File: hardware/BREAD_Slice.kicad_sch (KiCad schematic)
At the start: 14 parts, among them J1 Conn_01x10_Female

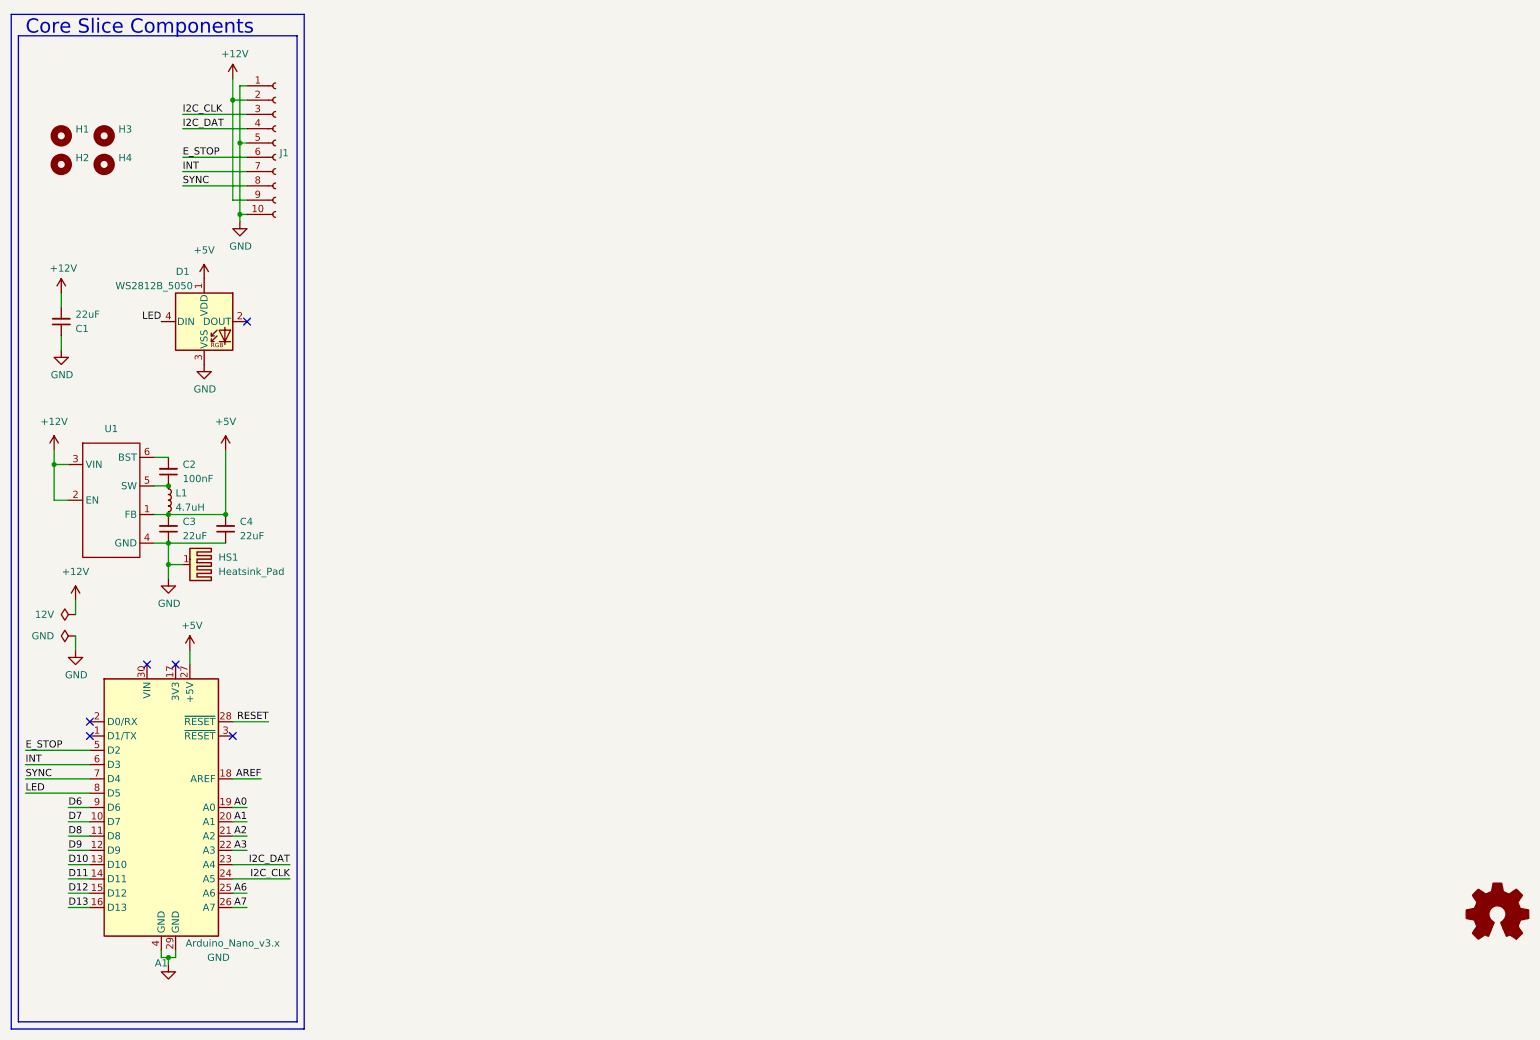
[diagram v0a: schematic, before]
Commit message: clear erc and drc but this board needs some rebuild help long term
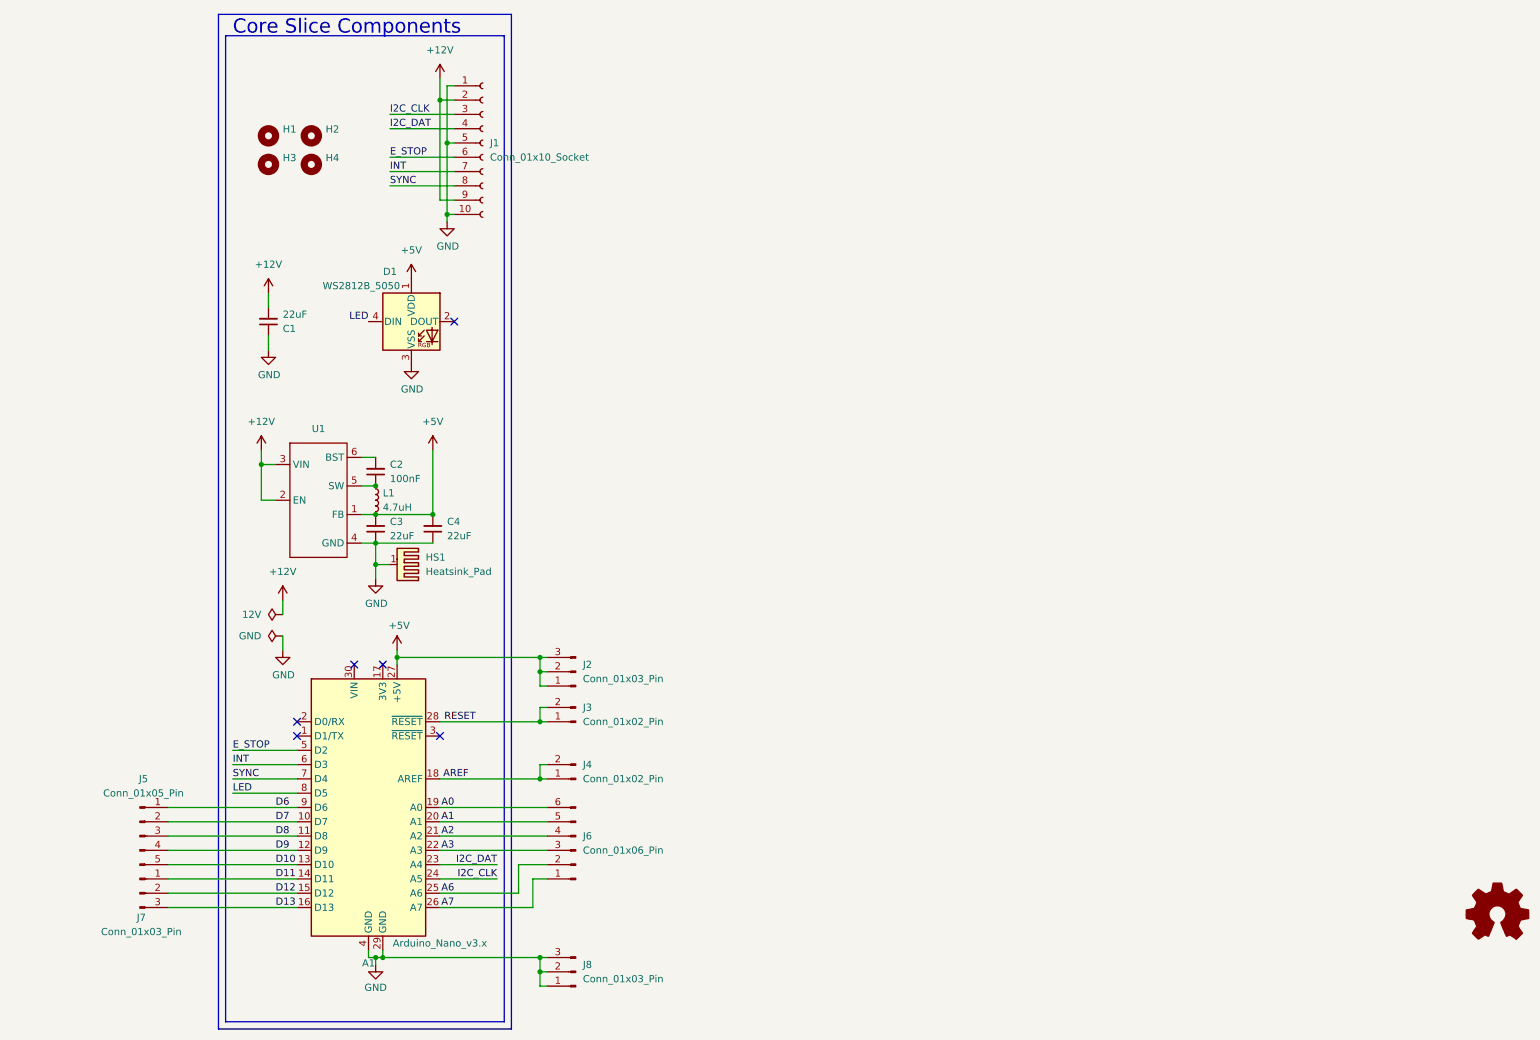
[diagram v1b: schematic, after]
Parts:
- removed J1: Conn_01x10_Female, Connector_PinSocket_2.54mm:PinSocket_1x10_P2.54mm_Horizontal, symbol Connector:Conn_01x10_Female
- added J1: Conn_01x10_Socket, Connector_PinSocket_2.54mm:PinSocket_1x10_P2.54mm_Horizontal, symbol Connector:Conn_01x10_Socket
- added J2, J7, J8: Conn_01x03_Pin, Connector_PinHeader_2.54mm:PinHeader_1x03_P2.54mm_Vertical, symbol Connector:Conn_01x03_Pin
- added J3, J4: Conn_01x02_Pin, Connector_PinHeader_2.54mm:PinHeader_1x02_P2.54mm_Vertical, symbol Connector:Conn_01x02_Pin
- added J5: Conn_01x05_Pin, Connector_PinHeader_2.54mm:PinHeader_1x05_P2.54mm_Vertical, symbol Connector:Conn_01x05_Pin
- added J6: Conn_01x06_Pin, Connector_PinHeader_2.54mm:PinHeader_1x06_P2.54mm_Vertical, symbol Connector:Conn_01x06_Pin
- renumbered H3 to H2, H2 to H3
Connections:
- net +12V: now also J1.2 (Pin_2), J1.9 (Pin_9)
- net +5V: now also J2.1 (Pin_1), J2.2 (Pin_2), J2.3 (Pin_3)
- net A0: now also J6.6 (Pin_6)
- net A1: now also J6.5 (Pin_5)
- net A2: now also J6.4 (Pin_4)
- net A3: now also J6.3 (Pin_3)
- net A6: now also J6.2 (Pin_2)
- net A7: now also J6.1 (Pin_1)
- net AREF: now also J4.1 (Pin_1), J4.2 (Pin_2)
- net D10: now also J5.5 (Pin_5)
- net D11: now also J7.1 (Pin_1)
- net D12: now also J7.2 (Pin_2)
- net D13: now also J7.3 (Pin_3)
- net D6: now also J5.1 (Pin_1)
- net D7: now also J5.2 (Pin_2)
- net D8: now also J5.3 (Pin_3)
- net D9: now also J5.4 (Pin_4)
- net E_STOP: now also J1.6 (Pin_6)
- net GND: now also J1.1 (Pin_1), J1.10 (Pin_10), J1.5 (Pin_5), J8.1 (Pin_1), J8.2 (Pin_2), J8.3 (Pin_3)
- net I2C_CLK: now also J1.3 (Pin_3)
- net I2C_DAT: now also J1.4 (Pin_4)
- net INT: now also J1.7 (Pin_7)
- net RESET: now also J3.1 (Pin_1), J3.2 (Pin_2)
- net SYNC: now also J1.8 (Pin_8)
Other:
- moved on the sheet: A1, C1, C2, C3, C4, D1, H1, H2, H3, H4, HS1, L1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
